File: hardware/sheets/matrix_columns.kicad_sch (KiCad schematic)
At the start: 0 parts

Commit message: hw: draw LED matrix, row and column drivers and scan-stall safety (#8)
* repo: ignore KiCad local history

KiCad 10 keeps automatic snapshots in a .history folder (with its own
Git repository) next to the project. Ignore it, and make the hygiene
check reject it, so local history cannot be committed.

* hw: save schematic sheets in KiCad's own format

Opening and saving the project in KiCad 10 rewrites the generated
sheets and project file in its native layout. KiCad also merges seven
overlapping wire segments on the USB sheet. Nets, values and
footprints are unchanged, so committing this once keeps later edits
made in KiCad free of formatting churn.

* hw: add column driver and monostable symbols

Add a TLC59283 symbol with the RGE (VQFN-24) pin numbers from TI's pin
table; it uses KiCad's footprint for TI's RGE0024C package. Add a
single-unit SN74LVC1G123 symbol, because KiCad's version keeps the
supply pins in a separate unit.

* hw: draw matrix driver and LED matrix sheets

Columns: two cascaded TLC59283 sinks on 3V3. R_IREF is 2.94k, an
18.0 mA nominal setting (about 19.4 mA worst case with driver and
resistor tolerance), with a fitted 0 ohm in series, so adjustment can
only lower the current.

Rows: the TLC chain output, clock, latch and SAFE cross into the LED
rail through an SN74LVC8T245 translator. Four SN74HC595 on VLED drive
32 AO3401A high-side switches with 10k gate pull-ups, with row
pull-downs as unfitted options.

Scan-stall safety: every latch retriggers an SN74LVC1G123. TI
specifies 1.0-1.1 ms at 10k / 0.1 uF; with the fitted parts'
tolerances the timeout is 0.76-1.41 ms. The part has only a Q
output, so an inverter makes SAFE = NOT Q. SAFE forces the column
BLANK through an OR gate and tri-states the row registers, and the
MCU reads it. The matrix stays dark while the MCU is off or in
reset.

LED matrix: 1024 LEDs, anodes on the rows and cathodes on the
columns, drawn as row and column buses, on the front side with the
buttons (ADR 0008).

The pend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
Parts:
- added C601, C603: 100nF, Capacitor_SMD:C_0402_1005Metric, symbol Device:C
- added C602, C604: 1uF, Capacitor_SMD:C_0402_1005Metric, symbol Device:C
- added R601, R603: 2.94k, Resistor_SMD:R_0402_1005Metric, symbol Device:R
- added R602, R604: 0, Resistor_SMD:R_0402_1005Metric, symbol Device:R
- added TP601: COL0, TestPoint:TestPoint_Pad_D1.0mm, symbol Connector:TestPoint
- added TP602: COL31, TestPoint:TestPoint_Pad_D1.0mm, symbol Connector:TestPoint
- added TP603: IREF1, TestPoint:TestPoint_Pad_D1.0mm, symbol Connector:TestPoint
- added TP604: IREF2, TestPoint:TestPoint_Pad_D1.0mm, symbol Connector:TestPoint
- added TP605: MTX_SCK, TestPoint:TestPoint_Pad_D1.0mm, symbol Connector:TestPoint
- added TP606: MTX_MOSI, TestPoint:TestPoint_Pad_D1.0mm, symbol Connector:TestPoint
- added TP607: MTX_LAT, TestPoint:TestPoint_Pad_D1.0mm, symbol Connector:TestPoint
- added U601, U602: TLC59283, Package_DFN_QFN:Texas_RGE0024C_VQFN-24-1EP_4x4mm_P0.5mm_EP2.1x2.1mm_ThermalVias, symbol smart-led-badge:TLC59283
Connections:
- new net +3V3: C601.1, C602.1, C603.1, C604.1, U601.21 (VCC), U602.21 (VCC)
- new net BLANK_TLC: U601.18 (BLANK), U602.18 (BLANK)
- new net COL0: TP601.1, U601.2 (OUT0)
- new net COL1: U601.3 (OUT1)
- new net COL10: U601.12 (OUT10)
- new net COL11: U601.13 (OUT11)
- new net COL12: U601.14 (OUT12)
- new net COL13: U601.15 (OUT13)
- new net COL14: U601.16 (OUT14)
- new net COL15: U601.17 (OUT15)
- new net COL16: U602.2 (OUT0)
- new net COL17: U602.3 (OUT1)
- new net COL18: U602.4 (OUT2)
- new net COL19: U602.5 (OUT3)
- new net COL2: U601.4 (OUT2)
- new net COL20: U602.6 (OUT4)
- new net COL21: U602.7 (OUT5)
- new net COL22: U602.8 (OUT6)
- new net COL23: U602.9 (OUT7)
- new net COL24: U602.10 (OUT8)
- new net COL25: U602.11 (OUT9)
- new net COL26: U602.12 (OUT10)
- new net COL27: U602.13 (OUT11)
- new net COL28: U602.14 (OUT12)
- new net COL29: U602.15 (OUT13)
- new net COL3: U601.5 (OUT3)
- new net COL30: U602.16 (OUT14)
- new net COL31: TP602.1, U602.17 (OUT15)
- new net COL4: U601.6 (OUT4)
- new net COL5: U601.7 (OUT5)
- new net COL6: U601.8 (OUT6)
- new net COL7: U601.9 (OUT7)
- new net COL8: U601.10 (OUT8)
- new net COL9: U601.11 (OUT9)
- new net GND: C601.2, C602.2, C603.2, C604.2, R602.2, R604.2, U601.22 (GND), U601.25 (EP), U602.22 (GND), U602.25 (EP)
- new net IREF1: R601.1, TP603.1, U601.20 (IREF)
- new net IREF1_LO: R601.2, R602.1
- new net IREF2: R603.1, TP604.1, U602.20 (IREF)
- new net IREF2_LO: R603.2, R604.1
- new net MTX_LAT: TP607.1, U601.1 (LAT), U602.1 (LAT)
- new net MTX_MISO: U602.19 (SOUT)
- new net MTX_MOSI: TP606.1, U601.23 (SIN)
- new net MTX_SCK: TP605.1, U601.24 (SCLK), U602.24 (SCLK)
- new net TLC_CHAIN: U601.19 (SOUT), U602.23 (SIN)
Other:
- note added: "Matrix column drivers (Rev A) - design notes 2 x TI TLC59283 (SBVS199C), RGE VQFN-24, VCC = 3V3, cascaded: MOSI -> U601 SIN, U601 SOUT -> U602 SIN, U602 SOUT -> MTX_MISO (SPIM4 readback) and the row-chain SER (row sheet). SCLK = MTX_SCK, LAT = MTX_LAT (also latches the row 595s). BLANK = BLANK_TLC = MTX_BLANK OR SAFE (row sheet); internal 500k pull-up on BLANK, 500k pull-down on LAT. R_IREF 2.94k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"

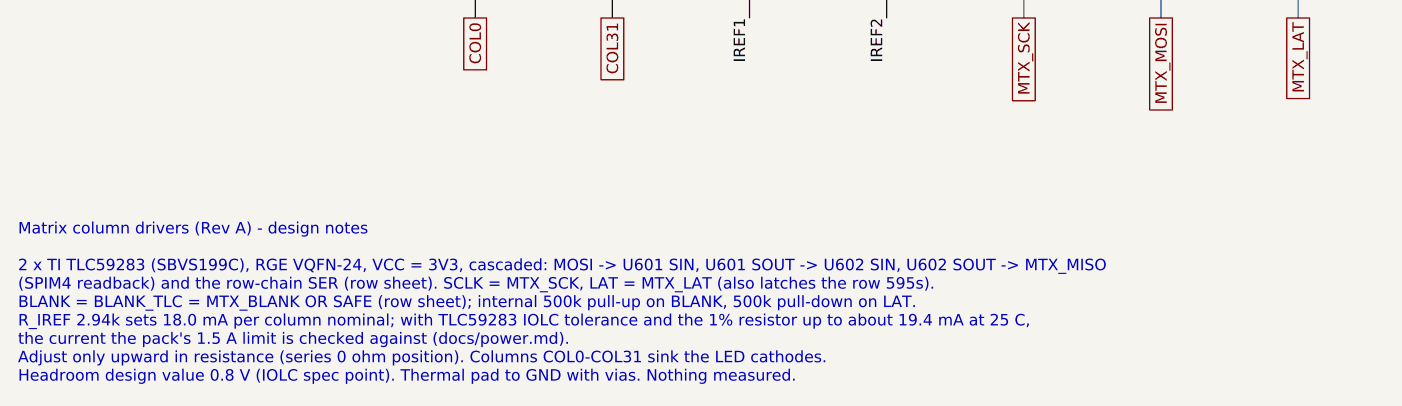
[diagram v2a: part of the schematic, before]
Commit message: hw: switch U401 to the E73 nRF52840 module
The MDBT53-P1M cannot be sourced in time for the Rev A order, while
the E73-2G4M08S1C is stocked at JLCPCB (ADR 0015).

The E73 holds its DC/DC inductors and decoupling, so L401/L402 and
C403/C404 are removed. The nRF52840 has no internal 32.768 kHz load,
so C405/C406 are fitted with 12 pF; the value is calculated and still
needs checking against the Product Specification. All 29 module GPIO
are used: CHG_STAT is no longer read by the MCU, and the UART pads,
spare GPIO pads and IMU SPI-fallback links are removed. Pins Ebyte
marks as low-frequency carry only analog inputs or slow signals.
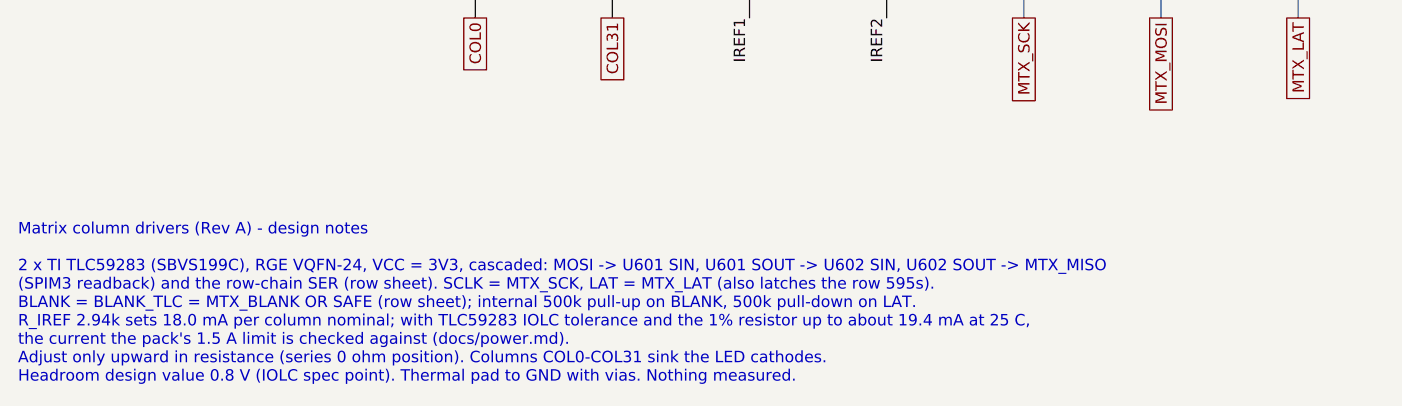
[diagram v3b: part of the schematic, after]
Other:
- note added: "Matrix column drivers (Rev A) - design notes 2 x TI TLC59283 (SBVS199C), RGE VQFN-24, VCC = 3V3, cascaded: MOSI -> U601 SIN, U601 SOUT -> U602 SIN, U602 SOUT -> MTX_MISO (SPIM3 readback) and the row-chain SER (row sheet). SCLK = MTX_SCK, LAT = MTX_LAT (also latches the row 595s). BLANK = BLANK_TLC = MTX_BLANK OR SAFE (row sheet); internal 500k pull-up on BLANK, 500k pull-down on LAT. R_IREF 2.94k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"
- note removed: "Matrix column drivers (Rev A) - design notes 2 x TI TLC59283 (SBVS199C), RGE VQFN-24, VCC = 3V3, cascaded: MOSI -> U601 SIN, U601 SOUT -> U602 SIN, U602 SOUT -> MTX_MISO (SPIM4 readback) and the row-chain SER (row sheet). SCLK = MTX_SCK, LAT = MTX_LAT (also latches the row 595s). BLANK = BLANK_TLC = MTX_BLANK OR SAFE (row sheet); internal 500k pull-up on BLANK, 500k pull-down on LAT. R_IREF 2.94k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"
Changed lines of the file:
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@@
 		(comment 2 "Schematic frozen for layout after review 2026-10-07; not for fabrication until the release gate")
 	)
-	(text "Matrix column drivers (Rev A) - design notes\n\n2 x TI TLC59283 (SBVS199C), RGE VQFN-24, VCC = 3V3, cascaded: MOSI -> U601 SIN, U601 SOUT -> U602 SIN, U602 SOUT -> MTX_MISO\n(SPIM4 readback) and the row-chain SER (row sheet). SCLK = MTX_SCK, LAT = MTX_LAT (also latches the row 595s).\nBLANK = BLANK_TLC = MTX_BLANK OR SAFE (row sheet); internal 500k pull-up on BLANK, 500k pull-down on LAT.\nR_IREF 2.94k sets 18.0 mA per column nominal; with TLC59283 IOLC tolerance and the 1% resistor up to about 19.4 mA at 25 C,\nthe current the pack's 1.5 A limit is checked against (docs/power.md).\nAdjust only upward in resistance (series 0 ohm position). Columns COL0-COL31 sink the LED cathodes.\nHeadroom design value 0.8 V (IOLC spec point). Thermal pad to GND with vias. Nothing measured."
+	(text "Matrix column drivers (Rev A) - design notes\n\n2 x TI TLC59283 (SBVS199C), RGE VQFN-24, VCC = 3V3, cascaded: MOSI -> U601 SIN, U601 SOUT -> U602 SIN, U602 SOUT -> MTX_MISO\n(SPIM3 readback) and the row-chain SER (row sheet). SCLK = MTX_SCK, LAT = MTX_LAT (also latches the row 595s).\nBLANK = BLANK_TLC = MTX_BLANK OR SAFE (row sheet); internal 500k pull-up on BLANK, 500k pull-down on LAT.\nR_IREF 2.94k sets 18.0 mA per column nominal; with TLC59283 IOLC tolerance and the 1% resistor up to about 19.4 mA at 25 C,\nthe current the pack's 1.5 A limit is checked against (docs/power.md).\nAdjust only upward in resistance (series 0 ohm position). Columns COL0-COL31 sink the LED cathodes.\nHeadroom design value 0.8 V (IOLC spec point). Thermal pad to GND with vias. Nothing measured."
 		(exclude_from_sim no)
 		(at 50.8 203.2 0)

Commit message: hw: lay out and route the Rev A board (#29)
* hw: add fab-layer references to custom footprints

Show each part's reference on F.Fab so the assembly drawing used for
bring-up and rework labels the custom parts the same way as the KiCad
library parts. Copper, courtyards and silkscreen are unchanged.

* hw: join the NFC coil's twin pad-2 ends as a jumper

The coil's inner and outer pad-2 ends are connected by footprint copper
(the In1 crossover), which KiCad does not count as a connection, so
NFC_LB stayed unrouted. Treat the duplicate pad numbers as a jumper.
The pad 1/2 net tie is unchanged.

* hw: remove unfitted parts and spare test points

Free routing room on the Rev A board:
- remove the eight DNP row pull-down arrays (RN709-RN716) and six DNP
  passive positions (C1103, R1005, R1104, R212, R213, R310)
- remove 19 test points outside the required set that had no room on
  the routed board

No net changes and no fitted-part changes, so the assembled board and
its BOM are the same. C1102 stays as the DNP NFC tuning position.

* hw: lay out and route the Rev A board

Place and route the 118 x 76 mm four-layer board: the 32 x 32 matrix at
45 degrees on the west, the row drivers in a column beside it, and the
power, charger, NFC, IMU, microphone and E73 module on the east. In1 is
a GND plane kept solid under the regulators, charger and module; a few
low-current signals cross it elsewhere where no other layer had room.
The board uses the JLC04161H-7628 stack-up, tented vias and
0.45/0.2 mm minimum vias.

Add release silkscreen: battery polarity at J302 on both faces,
test-point net names (front where they fit, rear behind each pad),
orientation-independent control marks, the board name and a designer
monogram on the NFC coil.

DRC and schematic parity are clean. Nothing is measured yet: charger,
USB, matrix timing, RF and NFC tuning remain bring-up checks. The README
and hardware docs now give the 118 x 76 mm outline.

* hw: move three vias out of component pads

The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
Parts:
- removed TP602: COL31, TestPoint:TestPoint_Pad_D1.0mm, symbol Connector:TestPoint
- removed TP603: IREF1, TestPoint:TestPoint_Pad_D1.0mm, symbol Connector:TestPoint
- removed TP604: IREF2, TestPoint:TestPoint_Pad_D1.0mm, symbol Connector:TestPoint
- removed TP606: MTX_MOSI, TestPoint:TestPoint_Pad_D1.0mm, symbol Connector:TestPoint
